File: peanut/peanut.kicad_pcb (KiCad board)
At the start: 4 copper layers, 81 parts, among them J1 USB-C, J2 PYRO_OUT, J3 Battery JST, J4 Arming, Q1 NMOS, Q2 NMOS, Q3 NMOS, Q4 NMOS, Q5 PMOS, U2 MS5611-01BA, U3 ESP32-C3FH4, U4 LM3671MF, U5 TPS2116DRL, Y1 32.768kHz, Y2 40MHz

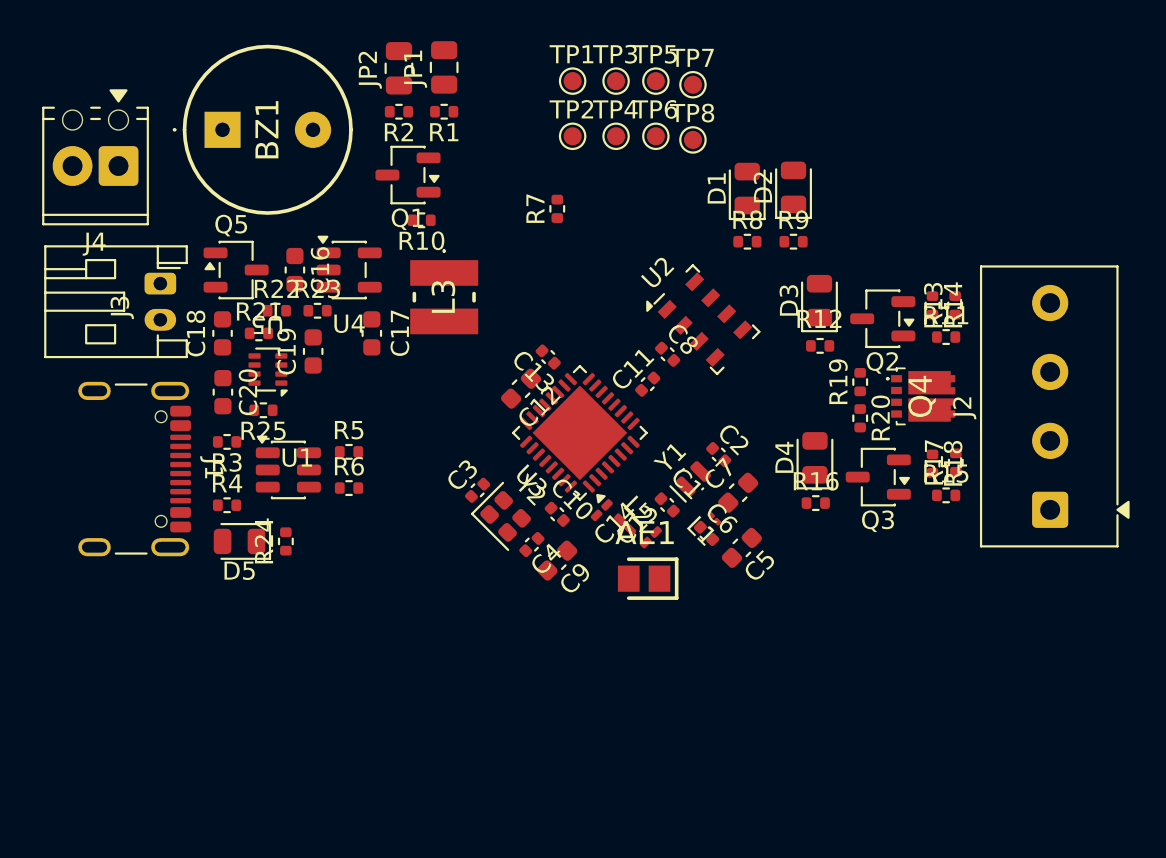
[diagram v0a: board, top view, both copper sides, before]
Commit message: bug: Fix missing connections to START/PANIC LEDs
The START/PANIC LEDs now take over the UART interface. If UART is
needed, using the pads of the LEDS should not be functionally different
than using the test points.
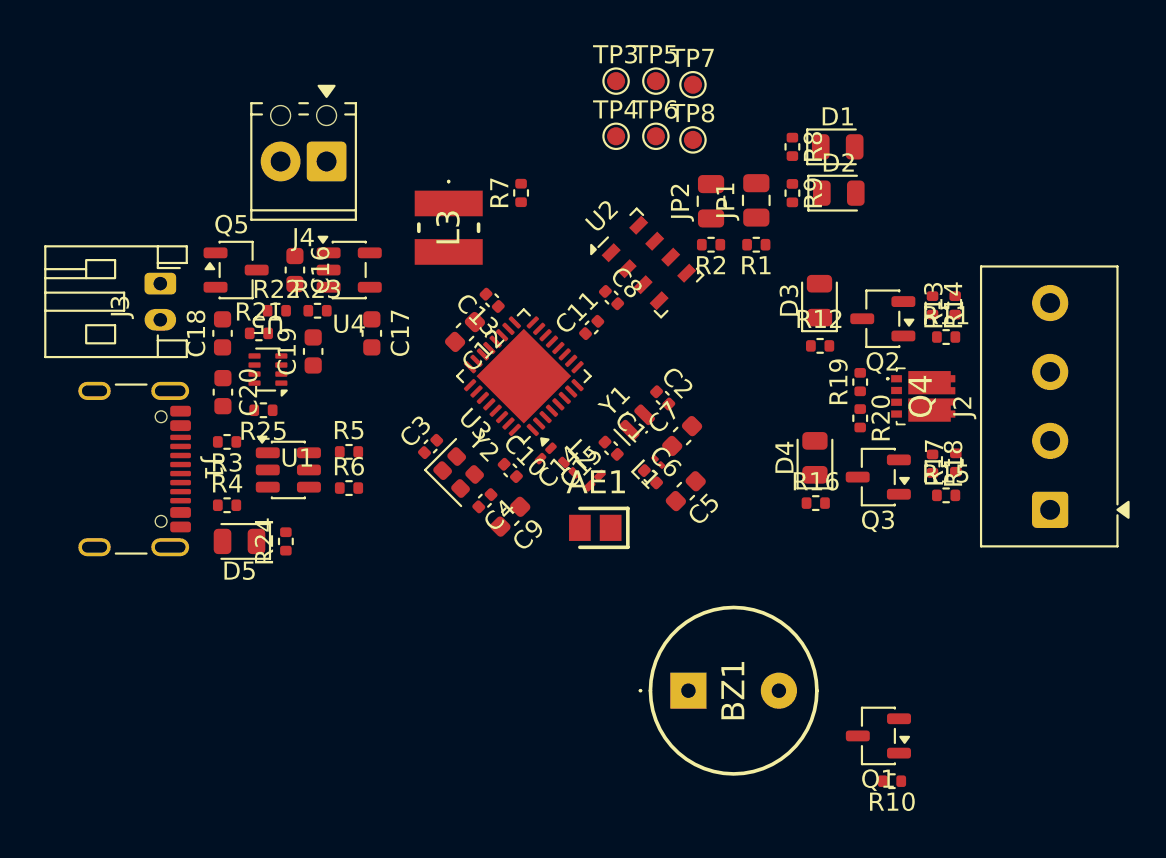
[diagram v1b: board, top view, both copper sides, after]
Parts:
- removed TP1: MCU_TX, TestPoint:TestPoint_Pad_D1.0mm
- removed TP2: MCU_RX, TestPoint:TestPoint_Pad_D1.0mm
- moved Q1 40.5 mm to (141.5, 115.0)
- moved R10 40.5 mm to (142.2, 117.5)
- moved BZ1 40.3 mm to (131.0, 112.5)
- moved JP1 18.8 mm to (134.8, 85.4)
- moved JP2 18.8 mm to (132.2, 85.4)
- moved R1 18.8 mm to (134.8, 87.8)
- moved R2 18.8 mm to (132.2, 87.8)
- moved J4 11.5 mm to (111.0, 83.2)
- moved R8 5.80 mm to (136.7, 82.4), turned to -90 degrees
- moved D1 5.51 mm to (139.2, 82.4), turned to 0 degrees
- moved C8 4.41 mm to (126.7, 90.8)
- moved U2 4.41 mm to (128.8, 88.9)
- moved C11 4.41 mm to (125.7, 92.4)
- moved C12 4.41 mm to (118.7, 92.7)
- moved C13 4.41 mm to (120.2, 90.9)
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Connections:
- U3 pad 27: /MCU_RX -> /PANIC
- U3 pad 28: /MCU_TX -> /START

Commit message: feat: Remove secondary crystal oscillator
We will rely on the internal crystal oscillator: it is cheaper, saves me
headaches routing the RF stuff and removes an unnecessary component.
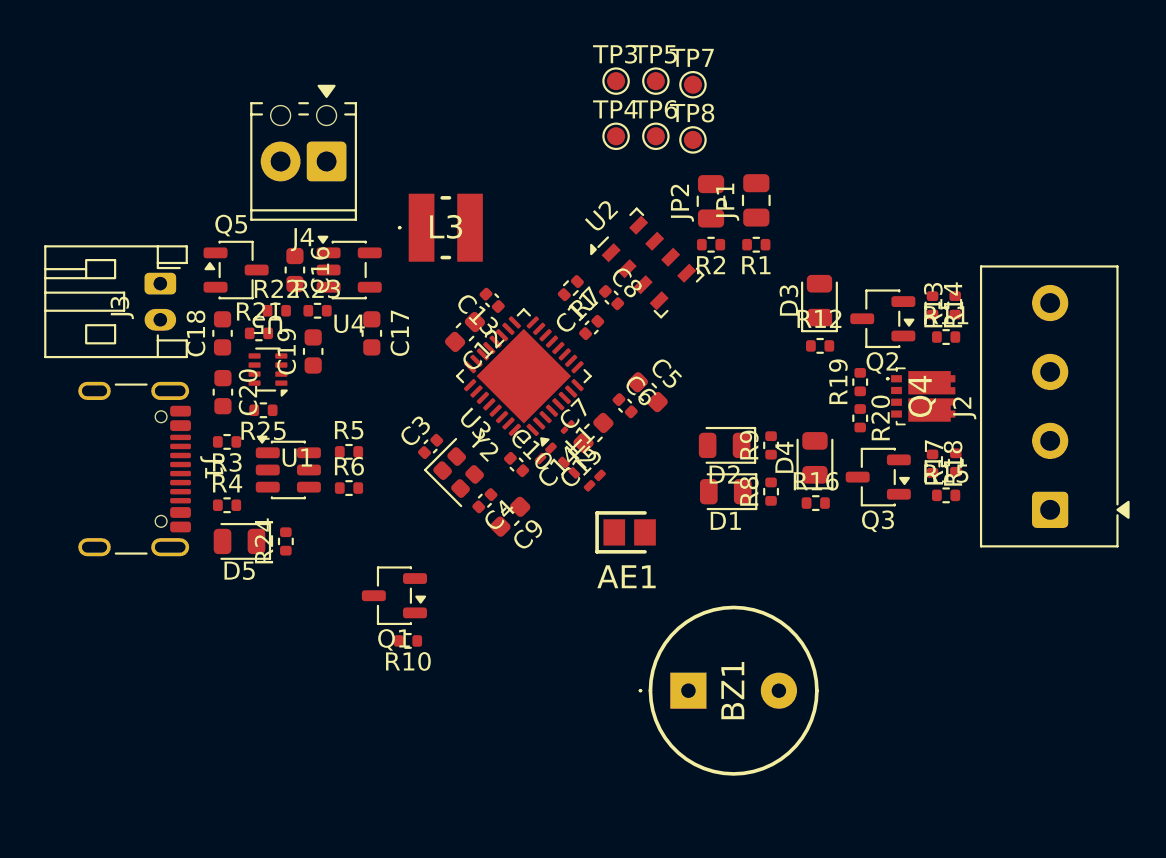
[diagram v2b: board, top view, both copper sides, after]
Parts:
- removed C1, C2: 18p, Capacitor_SMD:C_0402_1005Metric
- removed Y1: 32.768kHz, Crystal:Crystal_SMD_MicroCrystal_CM9V-T1A-2Pin_1.6x1.0mm
- moved Q1 27.9 mm to (114.8, 107.2)
- moved R10 27.9 mm to (115.5, 109.8)
- moved D1 20.0 mm to (133.1, 101.5), turned to 180 degrees
- moved R8 19.1 mm to (135.6, 101.5), turned to 90 degrees
- moved D2 15.3 mm to (133.0, 98.9), turned to 180 degrees
- moved R9 14.0 mm to (135.6, 98.9), turned to 90 degrees
- moved R7 5.94 mm to (124.5, 90.2), turned to -135 degrees
- moved C5 5.86 mm to (128.8, 96.0), turned to -45 degrees
- moved L1 5.36 mm to (124.3, 97.9), turned to -135 degrees
- moved C7 4.90 mm to (125.8, 98.2)
- moved C6 4.17 mm to (127.5, 96.8)
- moved AE1 1.92 mm to (127.8, 103.8), turned to 0 degrees
- moved C10 0.48 mm to (121.5, 100.0)
- moved L3 0.16 mm to (117.6, 86.9), turned to 0 degrees
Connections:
- U3 pad 4: /XL1 -> unconnected-(U3-XTAL_32K_P-Pad4)
- U3 pad 5: /XL2 -> unconnected-(U3-XTAL_32K_N-Pad5)

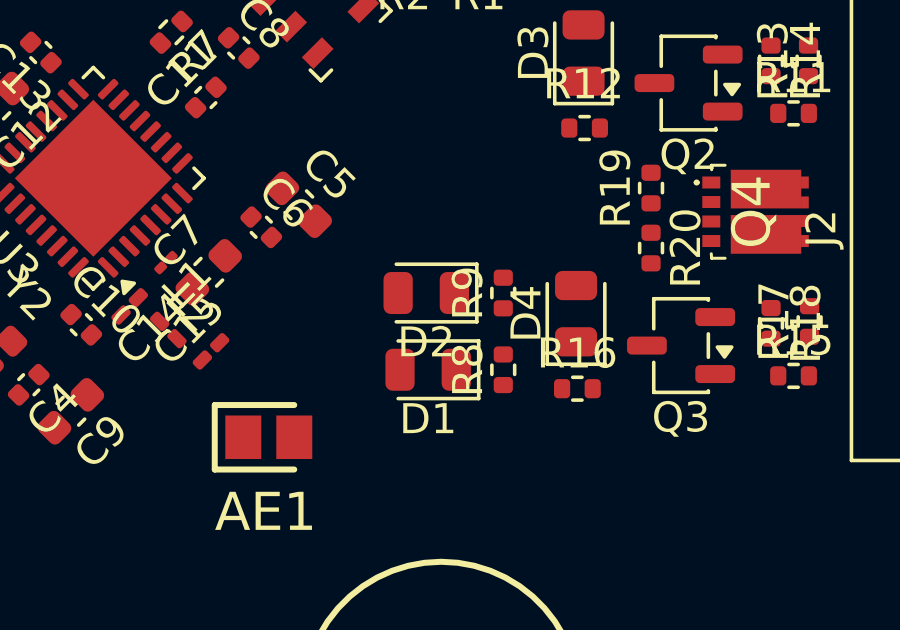
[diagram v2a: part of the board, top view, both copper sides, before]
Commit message: bug: Buzzer not connected
Fixed the buzzer line not being connected to anything by replacing the
PANIC LED with it. Buzzing during panic is equally acceptable, if not
annoying, while debugging.
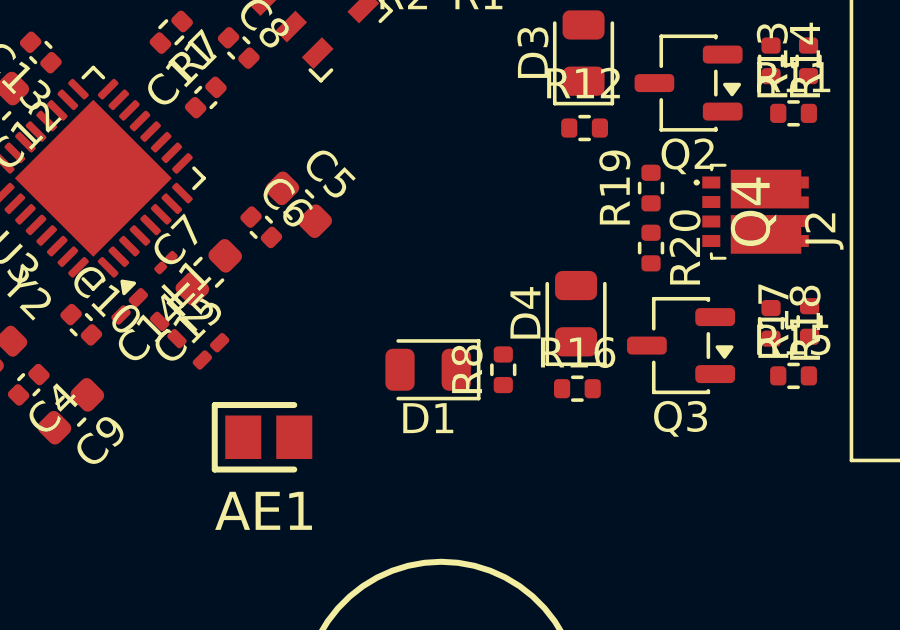
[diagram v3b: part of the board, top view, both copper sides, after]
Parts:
- removed D2: RED, LED_SMD:LED_0805_2012Metric
- removed R9: 330R, Resistor_SMD:R_0402_1005Metric
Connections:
- U3 pad 27: /PANIC -> /BUZ_PWM

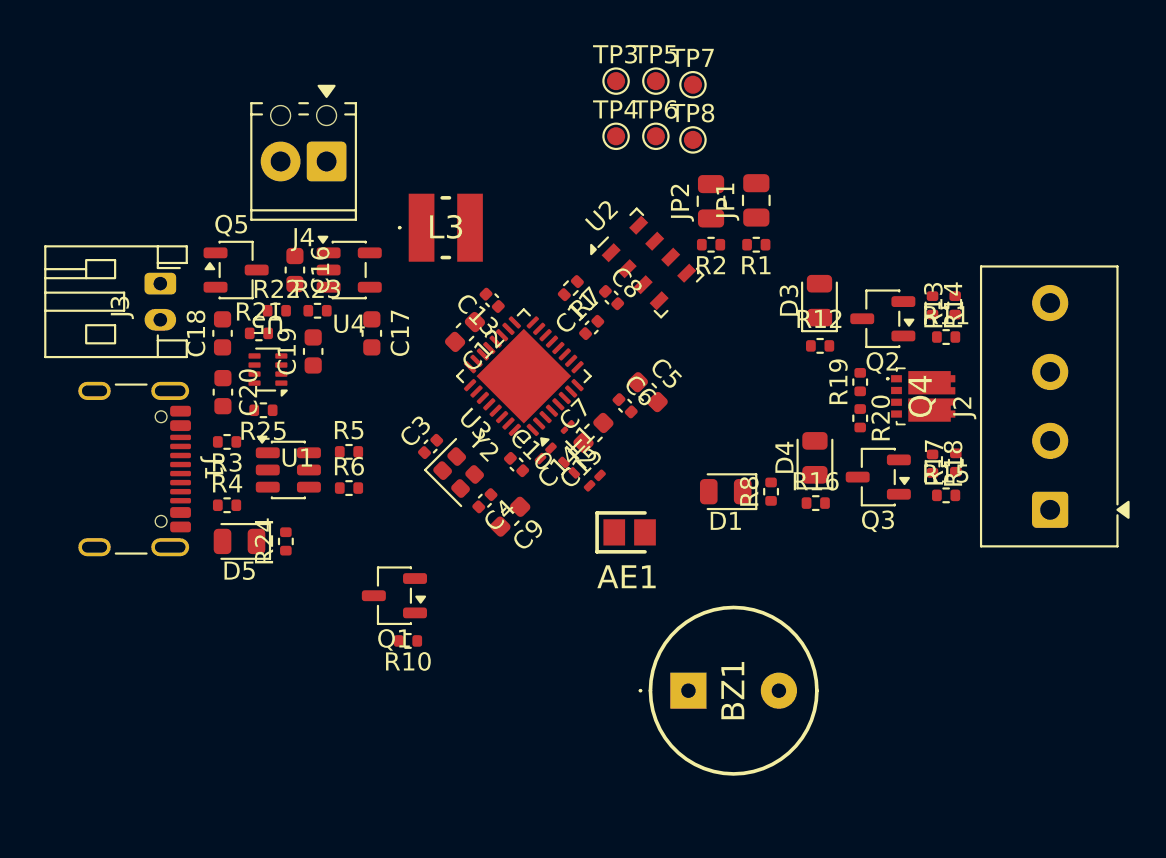
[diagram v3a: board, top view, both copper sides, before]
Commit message: feat: Mounting holes
Added M3 mounting holes.
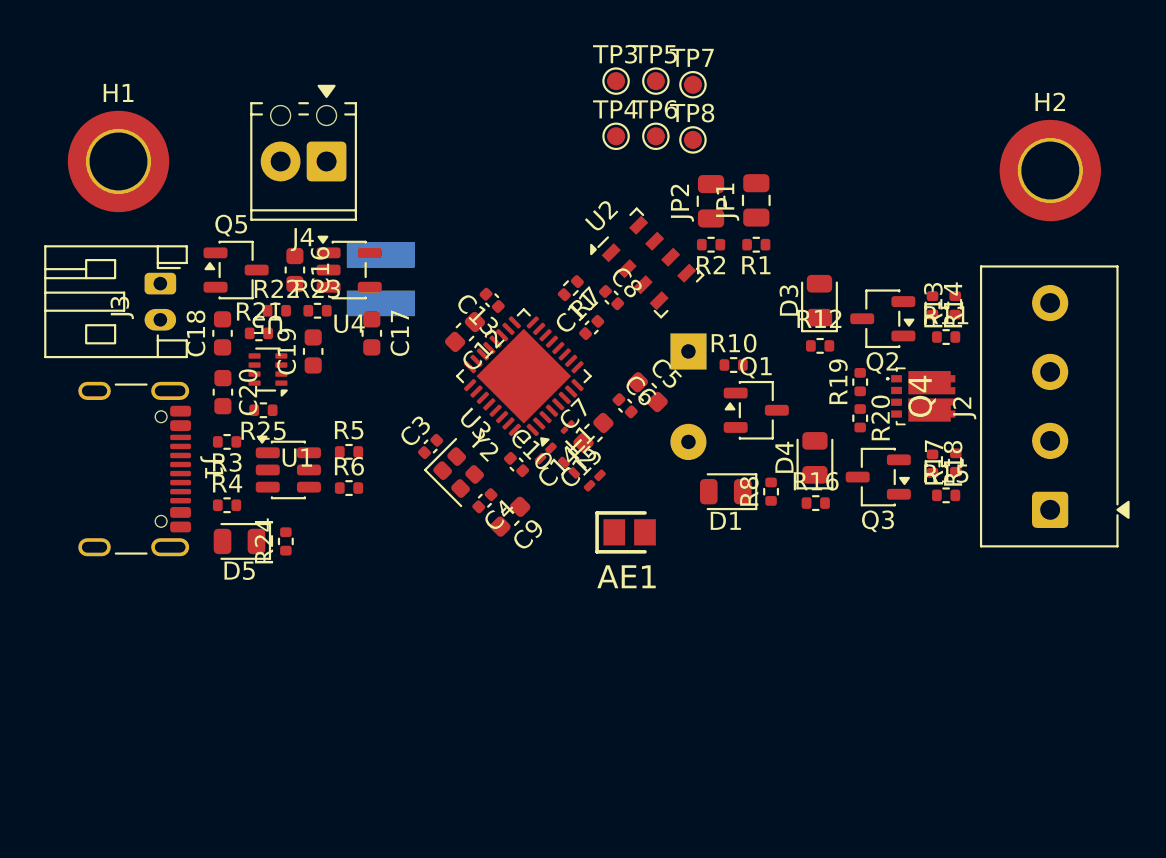
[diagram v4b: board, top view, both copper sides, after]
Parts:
- added H1: M3, MountingHole:MountingHole_3.2mm_M3_DIN965_Pad_TopOnly, F.Cu at (99.5, 83.2)
- added H2: M3, MountingHole:MountingHole_3.2mm_M3_DIN965_Pad_TopOnly, F.Cu at (151.0, 83.8)
- BZ1, L3: moved to B.Cu
- moved R10 23.6 mm to (133.5, 94.5), turned to 0 degrees
- moved Q1 22.5 mm to (134.8, 97.0), turned to 0 degrees
- moved BZ1 18.8 mm to (131.0, 93.8), turned to 180 degrees
- moved L3 4.58 mm to (114.0, 89.8), turned to -90 degrees

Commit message: feat: Better layout
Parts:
- removed TP3: 3V3, TestPoint:TestPoint_Pad_D1.0mm
- removed TP4: VBAT, TestPoint:TestPoint_Pad_D1.0mm
- removed TP5: VUSB, TestPoint:TestPoint_Pad_D1.0mm
- removed TP6: PWR_SRC, TestPoint:TestPoint_Pad_D1.0mm
- removed TP7: BAT+, TestPoint:TestPoint_Pad_D1.0mm
- removed TP8: GND, TestPoint:TestPoint_Pad_D1.0mm
- BZ1: moved to F.Cu
- C10, C17, C18, C19, C20, C5, C7, C9, Q1, Q2, Q3, Q5: moved to B.Cu
- moved JP1 28.3 mm to (107.0, 91.0)
- moved R1 28.3 mm to (107.0, 93.4)
- moved R2 28.3 mm to (104.5, 93.4)
- moved JP2 28.3 mm to (104.5, 91.0)
- moved H2 27.7 mm to (141.5, 109.8)
- moved R8 27.3 mm to (109.5, 93.5), turned to 0 degrees
- moved J4 26.4 mm to (106.2, 109.2), turned to 0 degrees
- moved D1 25.8 mm to (109.5, 91.0), turned to 90 degrees
- moved Q5 21.4 mm to (98.8, 109.4), turned to -90 degrees
- moved L3 19.9 mm to (114.2, 109.7)
- moved C16 19.7 mm to (111.8, 108.8)
- moved U4 19.7 mm to (114.8, 108.8)
- moved J3 18.5 mm to (102.0, 108.5)
- moved C17 17.7 mm to (118.2, 109.8), turned to 90 degrees
- moved R7 15.1 mm to (110.8, 96.5), turned to 0 degrees
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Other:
- board text added: "P1"
- board text added: "P2"

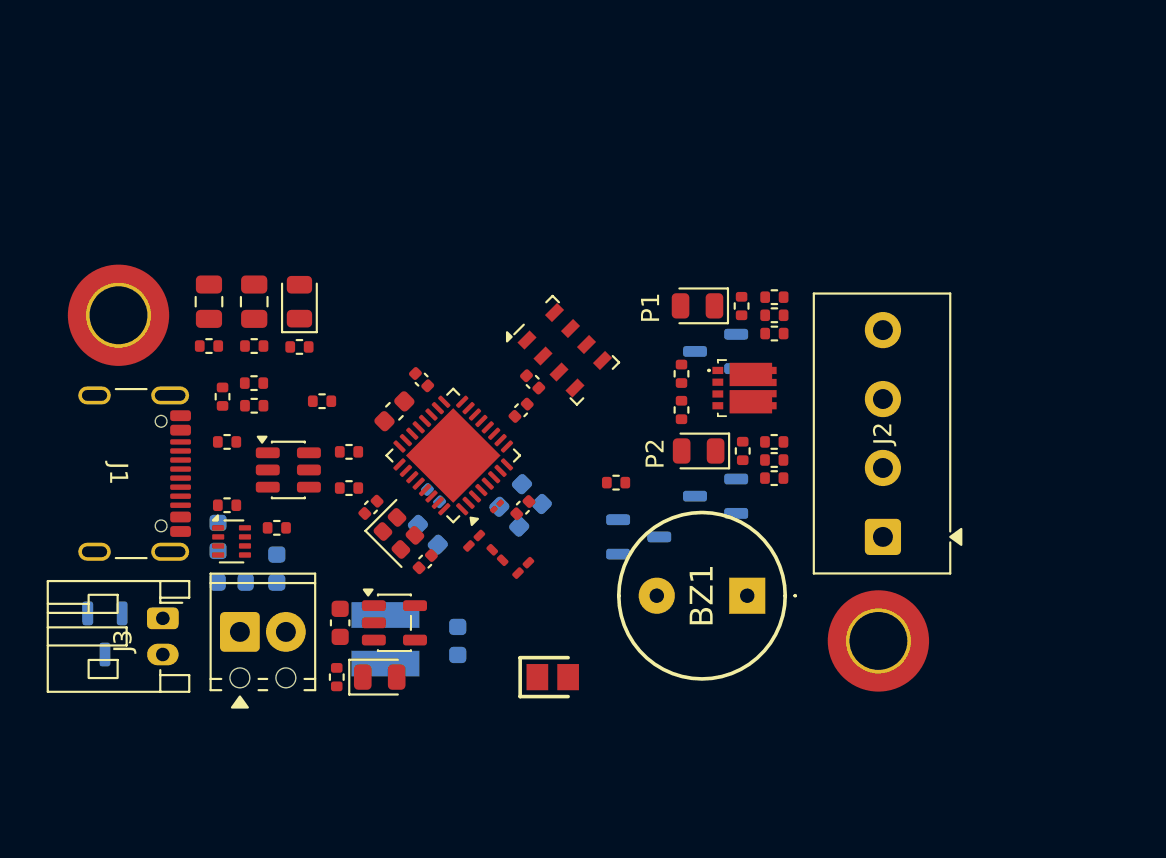
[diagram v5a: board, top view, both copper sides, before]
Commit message: feat: Added necessary silkscreen information
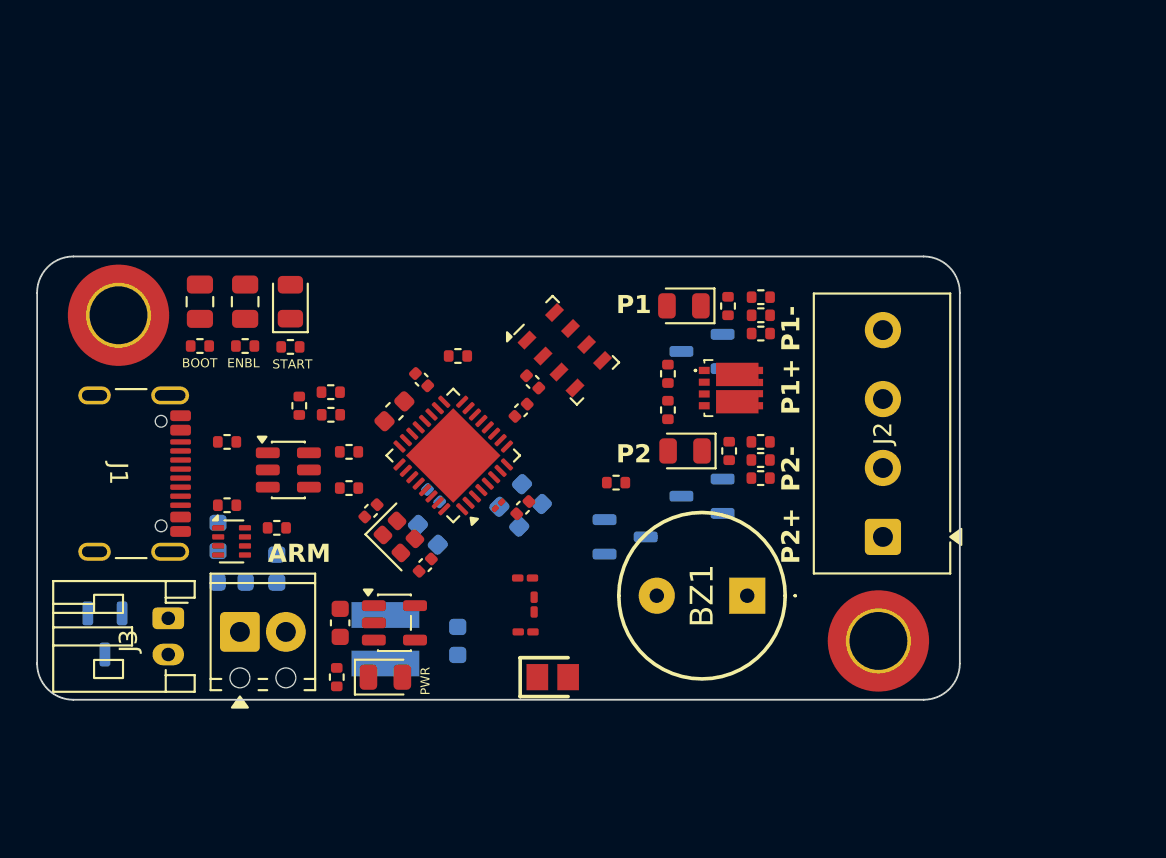
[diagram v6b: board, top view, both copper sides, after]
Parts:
- moved R8 7.92 mm to (118.3, 94.0)
- moved R20 4.27 mm to (111.2, 97.2)
- moved R22 4.27 mm to (109.5, 96.8)
- moved R21 4.27 mm to (111.2, 96.0)
- moved C13 3.54 mm to (122.0, 109.2), turned to 180 degrees
- moved C12 3.49 mm to (122.0, 106.3), turned to 180 degrees
- moved L2 3.41 mm to (122.5, 107.7), turned to -90 degrees
- moved D2 0.75 mm to (130.8, 91.2)
- moved D3 0.75 mm to (130.8, 99.2)
- moved Q1 0.75 mm to (127.5, 104.0)
- moved Q2 0.75 mm to (131.8, 93.8)
- moved Q3 0.75 mm to (131.8, 101.8)
- moved Q4 0.75 mm to (133.4, 95.8)
- moved R10 0.75 mm to (135.0, 92.8)
- moved R11 0.75 mm to (133.2, 91.2)
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- renumbered C3 to C1, C12 to C10, C13 to C11, C14 to C12, C15 to C13, C16 to C14, C17 to C15, C18 to C16, C19 to C17, C20 to C18, C4 to C2, C8 to C3, C5 to C4, C6 to C5, C7 to C6, C9 to C7, C10 to C8, C11 to C9, D3 to D2, D4 to D3, D5 to D4, R11 to R10, R12 to R11, R13 to R12, R14 to R13, R15 to R14, R16 to R15, R17 to R16, R18 to R17, R19 to R18, R20 to R19, R21 to R20, R22 to R21, R23 to R22, R24 to R23, R25 to R24, R8 to R7, R7 to R8, R10 to R9, U2 to U1, U1 to U2, Y2 to Y1
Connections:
- U3 pad 1: /LNA_IN -> /RF_LNA_IN
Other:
- board outline added: 51 x 24.5 mm
- board text added: "ARM"
- board text added: "BOOT"
- board text added: "ENBL"
- board text added: "P1+"
- board text added: "P1-"
- board text added: "P2+"
- board text added: "P2-"
- board text added: "PWR"
- board text added: "START"
